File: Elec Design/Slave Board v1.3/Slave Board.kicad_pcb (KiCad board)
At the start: 2 copper layers, 81.3 x 358.6 mm, 93 parts, among them J3 1935174, J6 61300411121, J7 Conn_ARM_JTAG_SWD_10, J8 1935161, J9 1935161, M1 VID28-05, M2 VID28-05, M3 VID28-05, M4 VID28-05, SW1 SW_SPST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

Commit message: updated schematic to fix buck fb point issue
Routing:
- net Net-(U14-SW): track 13.6 -> 8.95 mm
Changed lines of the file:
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@@
-	)
-	(segment
-		(start 214.554 179.832)
-		(end 217.869 176.517)
-		(width 0.25)
-		(layer "F.Cu")
-		(net 9)
 	)
 	(segment

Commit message: pre ketan updates
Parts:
- added C14: 0.1uF, Capacitor_SMD:C_0603_1608Metric, F.Cu at (238.0, 128.4)
- added C15: 0.1uF, Capacitor_SMD:C_0603_1608Metric, F.Cu at (239.9, 120.4)
- added C17: 0.1uF, Capacitor_SMD:C_0603_1608Metric, F.Cu at (250.8, 281.7)
- added C20: 0.1uF, Capacitor_SMD:C_0603_1608Metric, F.Cu at (249.3, 289.8)
- added R35: 10k, Resistor_SMD:R_0603_1608Metric, F.Cu at (239.1, 130.2)
- added R36: 10k, Resistor_SMD:R_0603_1608Metric, F.Cu at (249.8, 280.1)
- added U12: SN74LVC8T245, Package_SO:TSSOP-24_4.4x7.8mm_P0.65mm, F.Cu at (243.9, 125.1)
- added U13: SN74LVC8T245, Package_SO:TSSOP-24_4.4x7.8mm_P0.65mm, F.Cu at (245.0, 285.0)
- moved R29 93.8 mm to (244.6, 193.8)
- moved R30 93.3 mm to (247.7, 194.9)
- moved C30 11.4 mm to (210.1, 174.8), turned to 90 degrees
- moved C16 4.28 mm to (246.7, 196.5)
- moved R25 3.53 mm to (215.3, 175.6)
- moved R26 3.33 mm to (217.7, 174.7)
- moved C27 2.75 mm to (216.4, 191.0), turned to -90 degrees
- moved C5 2.66 mm to (243.5, 196.5), turned to 0 degrees
- moved C22 1.81 mm to (238.3, 291.3)
- moved C24 1.81 mm to (240.3, 291.3)
- moved C32 1.72 mm to (215.3, 174.0), turned to 0 degrees
- moved L1 1.31 mm to (212.1, 179.8), turned to 90 degrees
- moved C4 1.25 mm to (246.0, 215.8), turned to -90 degrees
- moved U15 1.02 mm to (214.7, 169.9)
- moved C31 0.74 mm to (211.7, 174.8), turned to 90 degrees
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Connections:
- R18 pad 1: +5V -> +3.3V
- R25 pad 1: Net-(U14-SW) -> +5V
- U2 pad 13: /CW/~{CCWC} - 1  -> Net-(U12-B5)
- U2 pad 14: /F(SCX)C - 1  -> Net-(U12-B6)
- U2 pad 16: /CW/~{CCWD} - 1 -> Net-(U12-B7)
- U2 pad 17: /F(SCX)D - 1  -> Net-(U12-B8)
- U2 pad 2: /CW/~{CCWB} - 1 -> Net-(U12-B3)
- U2 pad 27: /CW/~{CCWA} - 1 -> Net-(U12-B1)
- U2 pad 28: /F(SCX)A - 1  -> Net-(U12-B2)
- U2 pad 3: /F(SCX)B - 1  -> Net-(U12-B4)
- U3 pad 13: /CW/~{CCWC} - 2 -> Net-(U13-B5)
- U3 pad 14: /F(SCX)C - 2 -> Net-(U13-B6)
- U3 pad 16: /CW/~{CCWD} - 2 -> Net-(U13-B7)
- U3 pad 17: /F(SCX)D - 2 -> Net-(U13-B8)
- U3 pad 2: /CW/~{CCWB} - 2 -> Net-(U13-B3)
- U3 pad 27: /CW/~{CCWA} - 2 -> Net-(U13-B1)
- U3 pad 28: /F(SCX)A - 2 -> Net-(U13-B2)
- U3 pad 3: /F(SCX)B - 2 -> Net-(U13-B4)
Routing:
- net +3.3V: track 827.1 -> 868.6 mm, vias 12 -> 14
- net /CW/~{CCWC} - 2: track 126.3 -> 91.2 mm
- net /F(SCX)B - 2: track 109.9 -> 77.5 mm, vias 2 -> 0
- net /CW/~{CCWD} - 2: track 106.5 -> 76.2 mm
- net /CW/~{CCWB} - 2: track 106.5 -> 76.6 mm
- net Net-(U13-B6): track 0.00 -> 28.4 mm, vias 0 -> 2
- net /F(SCX)C - 2: track 115.6 -> 87.7 mm, vias 0 -> 2
- net Net-(U13-B7): track 0.00 -> 27.8 mm, vias 0 -> 2
- net Net-(U13-B8): track 0.00 -> 25.9 mm, vias 0 -> 2
- net /F(SCX)B - 1 : track 106.5 -> 80.8 mm
- net Net-(U13-B5): track 0.00 -> 24.9 mm
- net Net-(U12-B2): track 0.00 -> 24.6 mm, vias 0 -> 2
- net /CW/~{CCWA} - 1: track 121.2 -> 96.9 mm
- net /F(SCX)D - 2: track 114.1 -> 89.9 mm, vias 2 -> 0
- net Net-(U12-B1): track 0.00 -> 24.1 mm, vias 0 -> 2
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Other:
- board text added: "Slave Board V1.3"
- board text removed: "Slave Board V1.2"

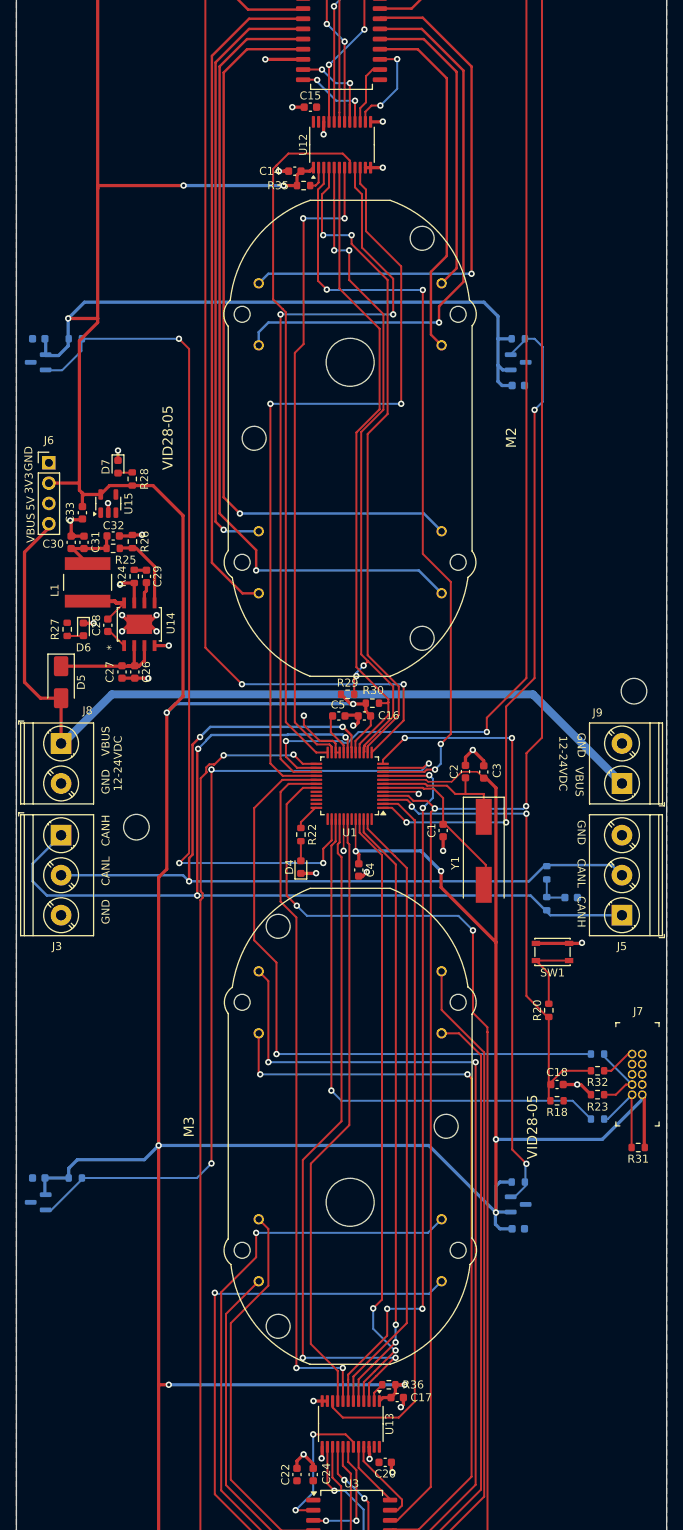
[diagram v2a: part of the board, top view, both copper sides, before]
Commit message: board layout changes - updates to buck converter layout
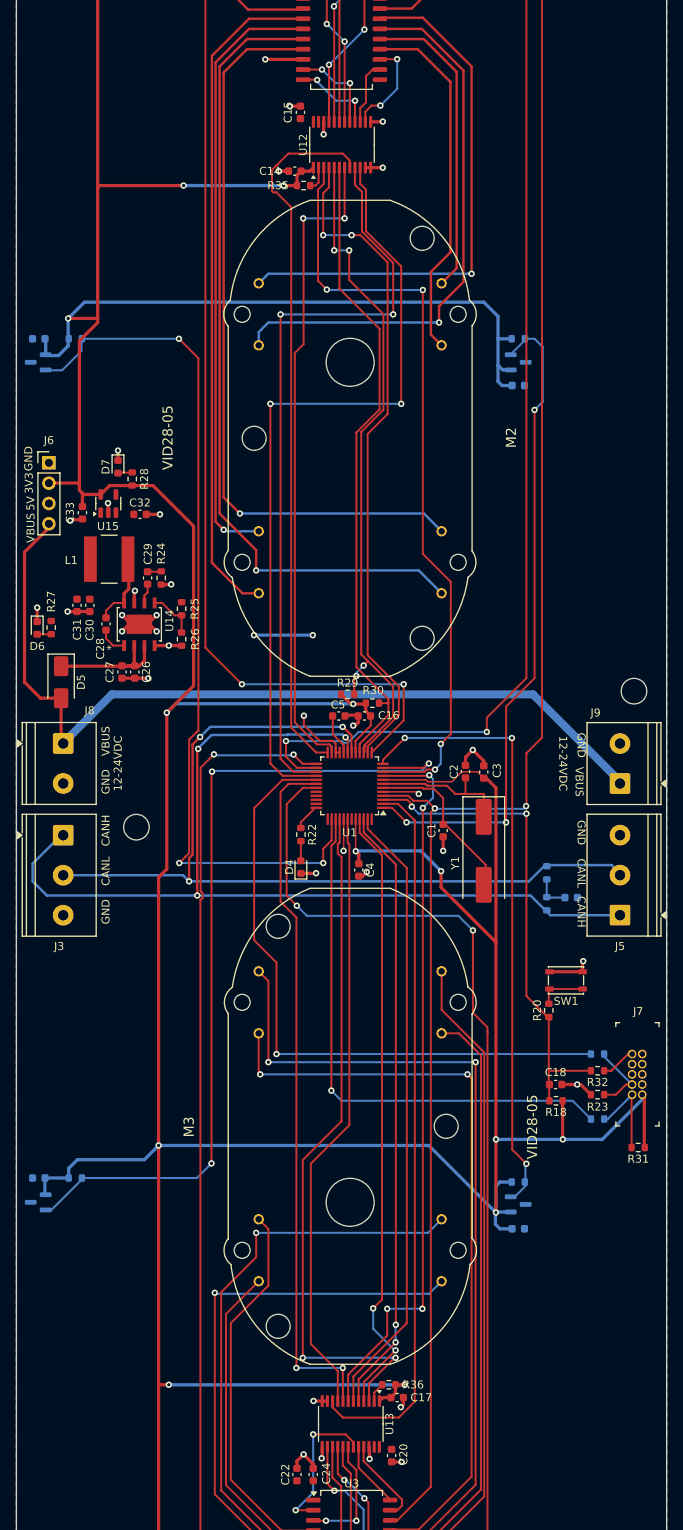
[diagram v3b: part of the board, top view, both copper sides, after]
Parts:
- moved R26 13.7 mm to (223.8, 186.9), turned to -90 degrees
- moved R25 11.4 mm to (223.8, 183.1), turned to -90 degrees
- moved C30 8.21 mm to (212.4, 182.7), turned to -90 degrees
- moved C31 7.92 mm to (210.8, 182.7), turned to -90 degrees
- moved D6 5.78 mm to (205.8, 185.5)
- moved C32 4.30 mm to (218.7, 171.3)
- moved L1 3.96 mm to (214.8, 176.9), turned to 180 degrees
- moved SW1 3.93 mm to (271.9, 229.6)
- moved R24 3.37 mm to (221.3, 179.2)
- moved R27 2.01 mm to (207.6, 185.4)
- moved C15 1.41 mm to (238.7, 121.0), turned to -90 degrees
- moved C20 1.17 mm to (250.1, 288.9), turned to 90 degrees
- moved C28 0.28 mm to (214.4, 185.0)
- moved J3 0.26 mm to (209.1, 211.4)
- moved J8 0.26 mm to (209.1, 199.9)
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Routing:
- net +3.3V: track 868.6 -> 874.6 mm, vias 14 -> 15
- net Net-(SW1-A): track 10.3 -> 6.03 mm
- net Net-(U14-FB): track 9.88 -> 5.97 mm
- net +5V: track 13.8 -> 12.6 mm, vias 0 -> 2
- net /HAll B Min - 1: track 109.7 -> 110.7 mm
- net Net-(U14-BOOT): track 3.12 -> 3.66 mm
- net Net-(U14-SW): track 8.08 -> 8.61 mm
- net GND: track 103.3 -> 102.8 mm, vias 36 -> 38
- net /F(SCX)A - 1 : track 83.2 -> 83.7 mm
- net /CANH: track 123.2 -> 123.7 mm
